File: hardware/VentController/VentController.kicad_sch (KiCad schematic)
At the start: 12 parts

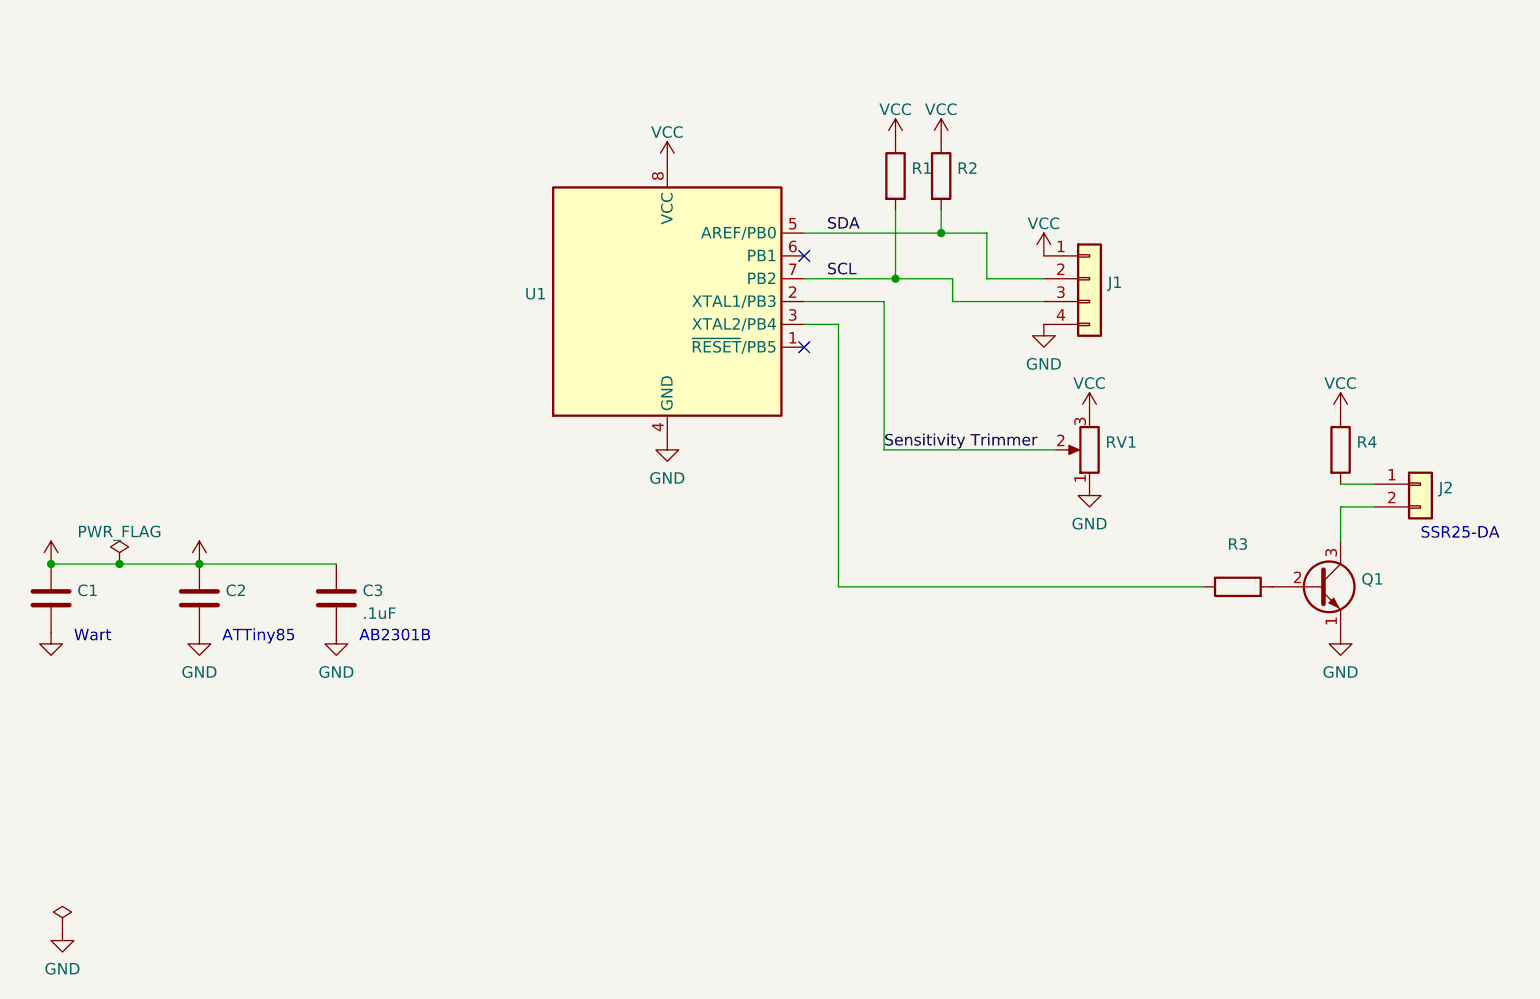
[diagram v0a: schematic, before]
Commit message: Add optional configurations to ssr
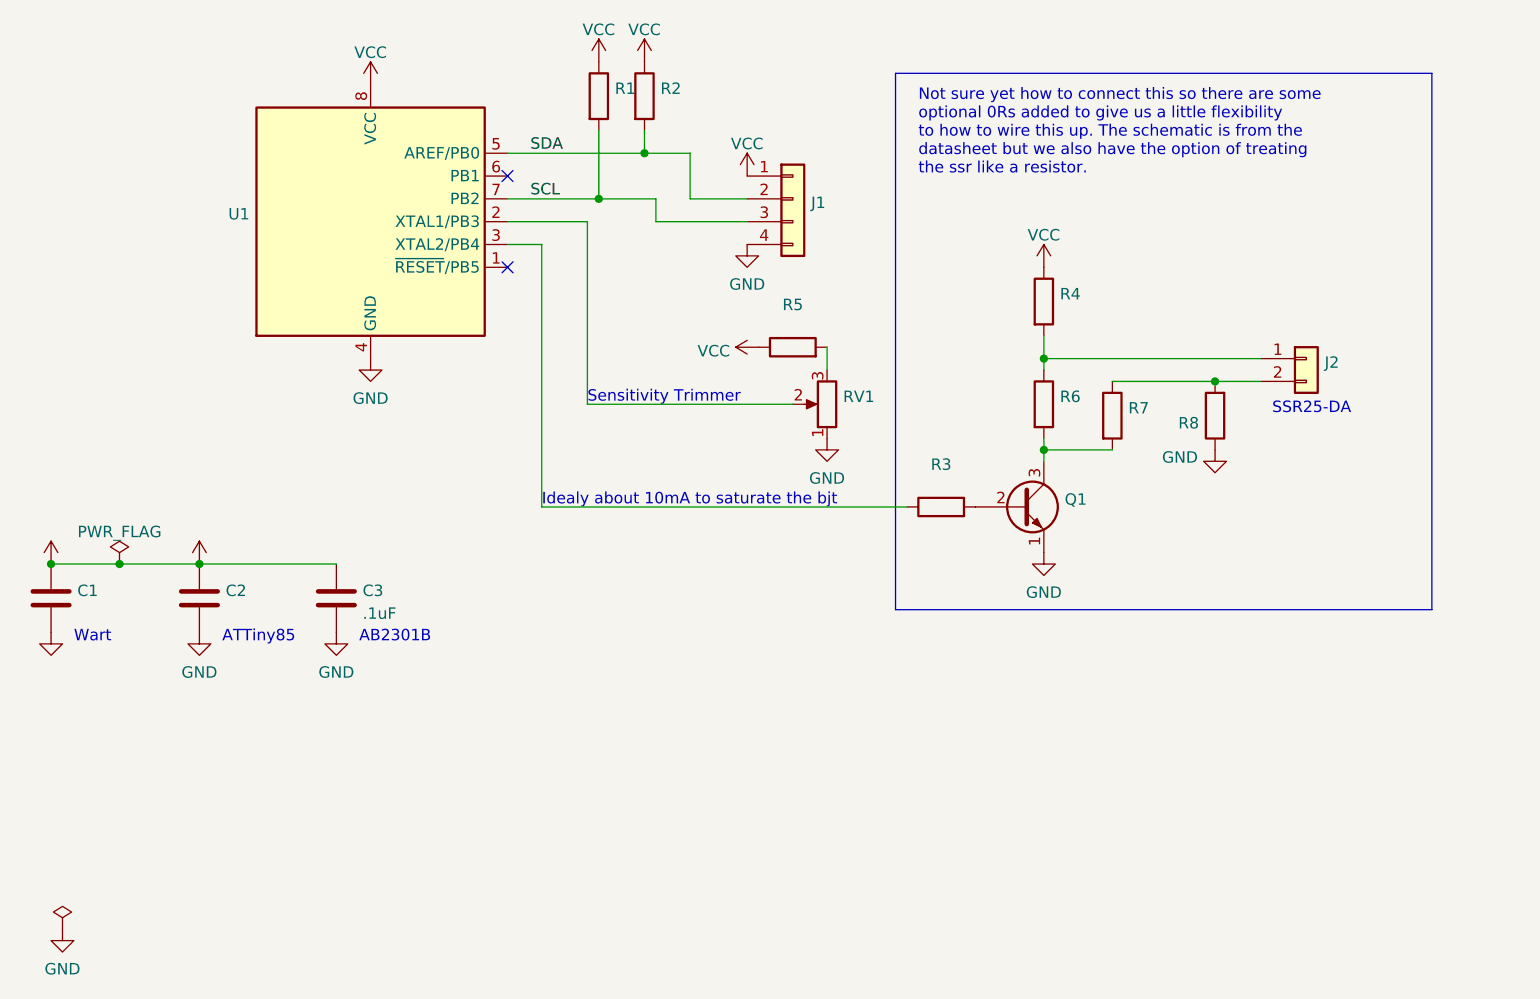
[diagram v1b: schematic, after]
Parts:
- added R5, R7, R8: (no value), Resistor_SMD:R_0805_2012Metric_Pad1.20x1.40mm_HandSolder, symbol Device:R
- added R6: (no value), symbol Device:R
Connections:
- net +5V: now also R5.1; no longer RV1.3
- net GND: now also R8.1
- net at J2.1 (Pin_1), R4.2: now also R6.1
- net at J2.2 (Pin_2): now also R7.1, R8.2; no longer Q1.3 (C)
- net Sensitivity Trimmer: no longer names the net of RV1.2, U1.2 (XTAL1/PB3)
- new net: R5.2, RV1.3
- new net: Q1.3 (C), R6.2, R7.2
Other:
- note added: "Idealy about 10mA to saturate the bjt"
- note added: "Not sure yet how to connect this so there are some optional 0Rs added to give us a little flexibility to how to wire this up. The schematic is from the datasheet but we also have the option of treating the ssr like a resistor."
- note added: "Sensitivity Trimmer"
- moved on the sheet: J1, J2, Q1, R1, R2, R3, R4, RV1, U1

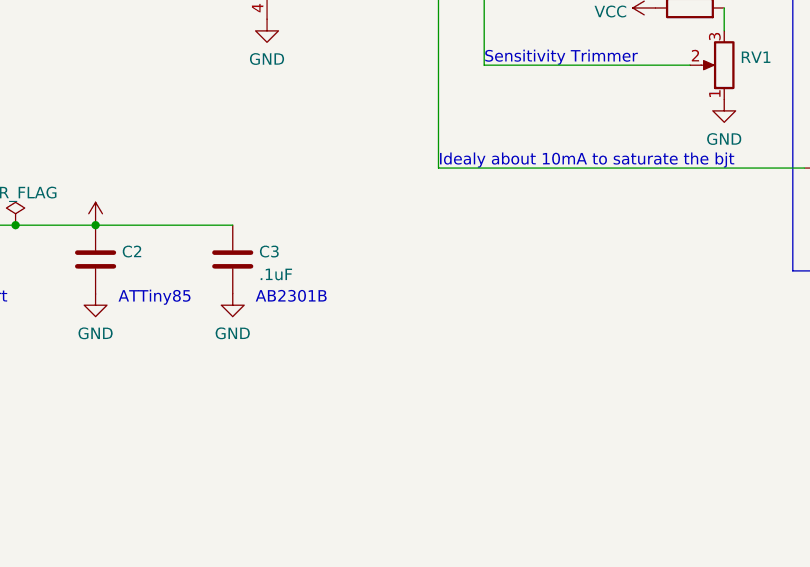
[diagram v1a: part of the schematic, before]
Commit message: Add decoupling caps for ssr and trimmer
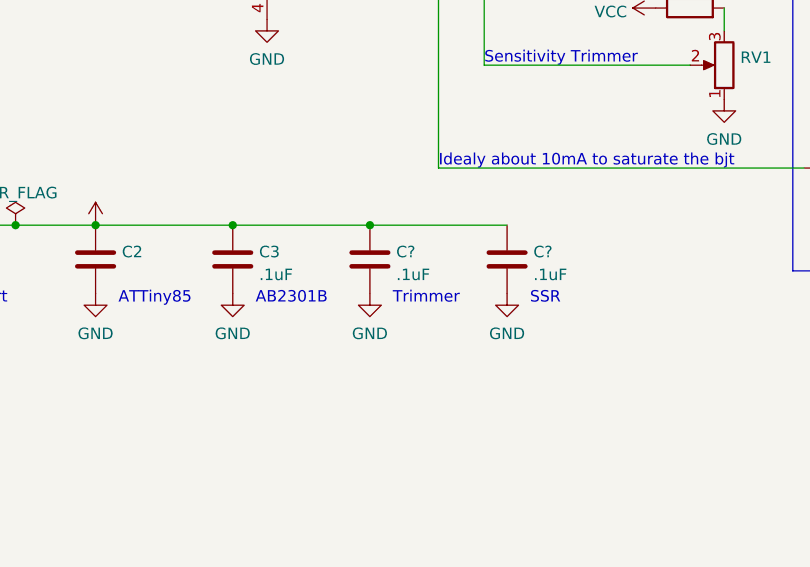
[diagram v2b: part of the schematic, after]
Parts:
- added C? (x2): .1uF, Capacitor_SMD:C_0805_2012Metric_Pad1.18x1.45mm_HandSolder, symbol Device:C
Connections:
- net +5V: now also C?.1, C?.1
- net GND: now also C?.2, C?.2
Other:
- note added: "SSR"
- note added: "Trimmer"
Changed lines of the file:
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@@
   (junction (at 92.71 34.29) (diameter 0) (color 0 0 0 0)
   )
+  (junction (at 58.42 80.01) (diameter 0) (color 0 0 0 0)
+  )
   (junction (at 137.16 57.15) (diameter 0) (color 0 0 0 0)
   )
   (junction (at 34.29 80.01) (diameter 0) (color 0 0 0 0)
+  )
+  (junction (at 73.66 80.01) (diameter 0) (color 0 0 0 0)
   )
   (junction (at 156.21 59.69) (diameter 0) (color 0 0 0 0)
@@
     (stroke (width 0) (type default) (color 0 0 0 0))
   )
+  (wire (pts (xy 73.66 80.01) (xy 88.9 80.01))
+    (stroke (width 0) (type default) (color 0 0 0 0))
+  )
   (wire (pts (xy 86.36 62.23) (xy 109.22 62.23))
     (stroke (width 0) (type default) (color 0 0 0 0))
@@
   )
   (wire (pts (xy 77.47 39.37) (xy 87.63 39.37))
+    (stroke (width 0) (type default) (color 0 0 0 0))
+  )
+  (wire (pts (xy 58.42 80.01) (xy 73.66 80.01))
     (stroke (width 0) (type default) (color 0 0 0 0))
   )
@@
     )
   )
+  (text "Trimmer\n" (at 76.2 88.9 0)
+    (effects (font (size 1.27 1.27)) (justify left bottom))
+  )
   (text "Sensitivity Trimmer" (at 86.36 62.23 0)
     (effects (font (size 1.27 1.27)) (justify left bottom))
@@
   )
   (text "Wart" (at 29.21 88.9 0)
+    (effects (font (size 1.27 1.27)) (justify left bottom))
+  )
+  (text "SSR\n" (at 91.44 88.9 0)
     (effects (font (size 1.27 1.27)) (justify left bottom))
   )
@@
     (pin "1")
   )
+  (symbol (lib_id "power:GND") (at 88.9 87.63 0) (unit 1)
+    (in_bom yes) (on_board yes) (fields_autoplaced)
+    (property "Reference" "#PWR?" (id 0) (at 88.9 93.98 0)
+      (effects (font (size 1.27 1.27)) hide)
+    )
+    (property "Value" "GND" (id 1) (at 88.9 92.0734 0))
+    (property "Footprint" "" (id 2) (at 88.9 87.63 0)
+      (effects (font (size 1.27 1.27)) hide)
+    )
+    (property "Datasheet" "" (id 3) (at 88.9 87.63 0)
+      (effects (font (size 1.27 1.27)) hide)
+    )
+    (pin "1")
+  )
   (symbol (lib_id "power:GND") (at 113.03 66.04 0) (unit 1)
     (in_bom yes) (on_board yes) (fields_autoplaced)
@@
     (pin "2")
   )
+  (symbol (lib_id "Device:C") (at 73.66 83.82 0) (unit 1)
+    (in_bom yes) (on_board yes) (fields_autoplaced)
+    (property "Reference" "C?" (id 0) (at 76.581 82.9853 0)
+      (effects (font (size 1.27 1.27)) (justify left))
+    )
+    (property "Value" ".1uF" (id 1) (at 76.581 85.5222 0)
+      (effects (font (size 1.27 1.27)) (justify left))
+    )
+    (property "Footprint" "Capacitor_SMD:C_0805_2012Metric_Pad1.18x1.45mm_HandSolder" (id 2) (at 74.6252 87.63 0)
+      (effects (font (size 1.27 1.27)) hide)
+    )
+    (property "Datasheet" "~" (id 3) (at 73.66 83.82 0)
+      (effects (font (size 1.27 1.27)) hide)
+    )
+    (pin "1")
+    (pin "2")
+  )
   (symbol (lib_id "power:GND") (at 58.42 87.63 0) (unit 1)
     (in_bom yes) (on_board yes) (fields_autoplaced)
@@
     (pin "2")
   )
+  (symbol (lib_id "power:GND") (at 73.66 87.63 0) (unit 1)
+    (in_bom yes) (on_board yes) (fields_autoplaced)
+    (property "Reference" "#PWR?" (id 0) (at 73.66 93.98 0)
+      (effects (font (size 1.27 1.27)) hide)
+    )
+    (property "Value" "GND" (id 1) (at 73.66 92.0734 0))
+    (property "Footprint" "" (id 2) (at 73.66 87.63 0)
+      (effects (font (size 1.27 1.27)) hide)
+    )
+    (property "Datasheet" "" (id 3) (at 73.66 87.63 0)
+      (effects (font (size 1.27 1.27)) hide)
+    )
+    (pin "1")
+  )
+  (symbol (lib_id "Device:C") (at 88.9 83.82 0) (unit 1)
+    (in_bom yes) (on_board yes) (fields_autoplaced)
+    (property "Reference" "C?" (id 0) (at 91.821 82.9853 0)
+      (effects (font (size 1.27 1.27)) (justify left))
+    )
+    (property "Value" ".1uF" (id 1) (at 91.821 85.5222 0)
+      (effects (font (size 1.27 1.27)) (justify left))
+    )
+    (property "Footprint" "Capacitor_SMD:C_0805_2012Metric_Pad1.18x1.45mm_HandSolder" (id 2) (at 89.8652 87.63 0)
+      (effects (font (size 1.27 1.27)) hide)
+    )
+    (property "Datasheet" "~" (id 3) (at 88.9 83.82 0)
+      (effects (font (size 1.27 1.27)) hide)
+    )
+    (pin "1")
+    (pin "2")
+  )
   (sheet_instances
     (path "/" (page "1"))
@@
       (reference "#PWR017") (unit 1) (value "GND") (footprint "")
     )
+    (path "/65b883a7-f8ee-466f-b815-3a02492bdf71"
+      (reference "#PWR?") (unit 1) (value "GND") (footprint "")
+    )
+    (path "/fc6cb265-d9be-4c2b-ab77-dd6c5935e9d5"
+      (reference "#PWR?") (unit 1) (value "GND") (footprint "")
+    )
     (path "/f81e2caa-f7a2-40dd-8668-c447b8223c0a"
       (reference "C1") (unit 1) (value "1uF") (footprint "Capacitor_SMD:C_0805_2012Metric_Pad1.18x1.45mm_HandSolder")
@@
       (reference "C3") (unit 1) (value ".1uF") (footprint "Capacitor_SMD:C_0805_2012Metric_Pad1.18x1.45mm_HandSolder")
     )
+    (path "/bb3c9ed5-e3f9-4498-b24a-1898528d46d5"
+      (reference "C?") (unit 1) (value ".1uF") (footprint "Capacitor_SMD:C_0805_2012Metric_Pad1.18x1.45mm_HandSolder")
+    )
+    (path "/fcd0c6b2-8872-4fcb-ae27-f6c287e9791c"
+      (reference "C?") (unit 1) (value ".1uF") (footprint "Capacitor_SMD:C_0805_2012Metric_Pad1.18x1.45mm_HandSolder")
+    )
     (path "/a0c0156d-8f3c-4c82-999f-49c9d8d8e545"

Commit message: Add power jack
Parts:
- added J3: (no value), symbol Connector:Barrel_Jack
- gave numbers to parts that had none: 2
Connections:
- net +5V: now also J3.1
- net GND: now also J3.2
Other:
- moved on the sheet: R2

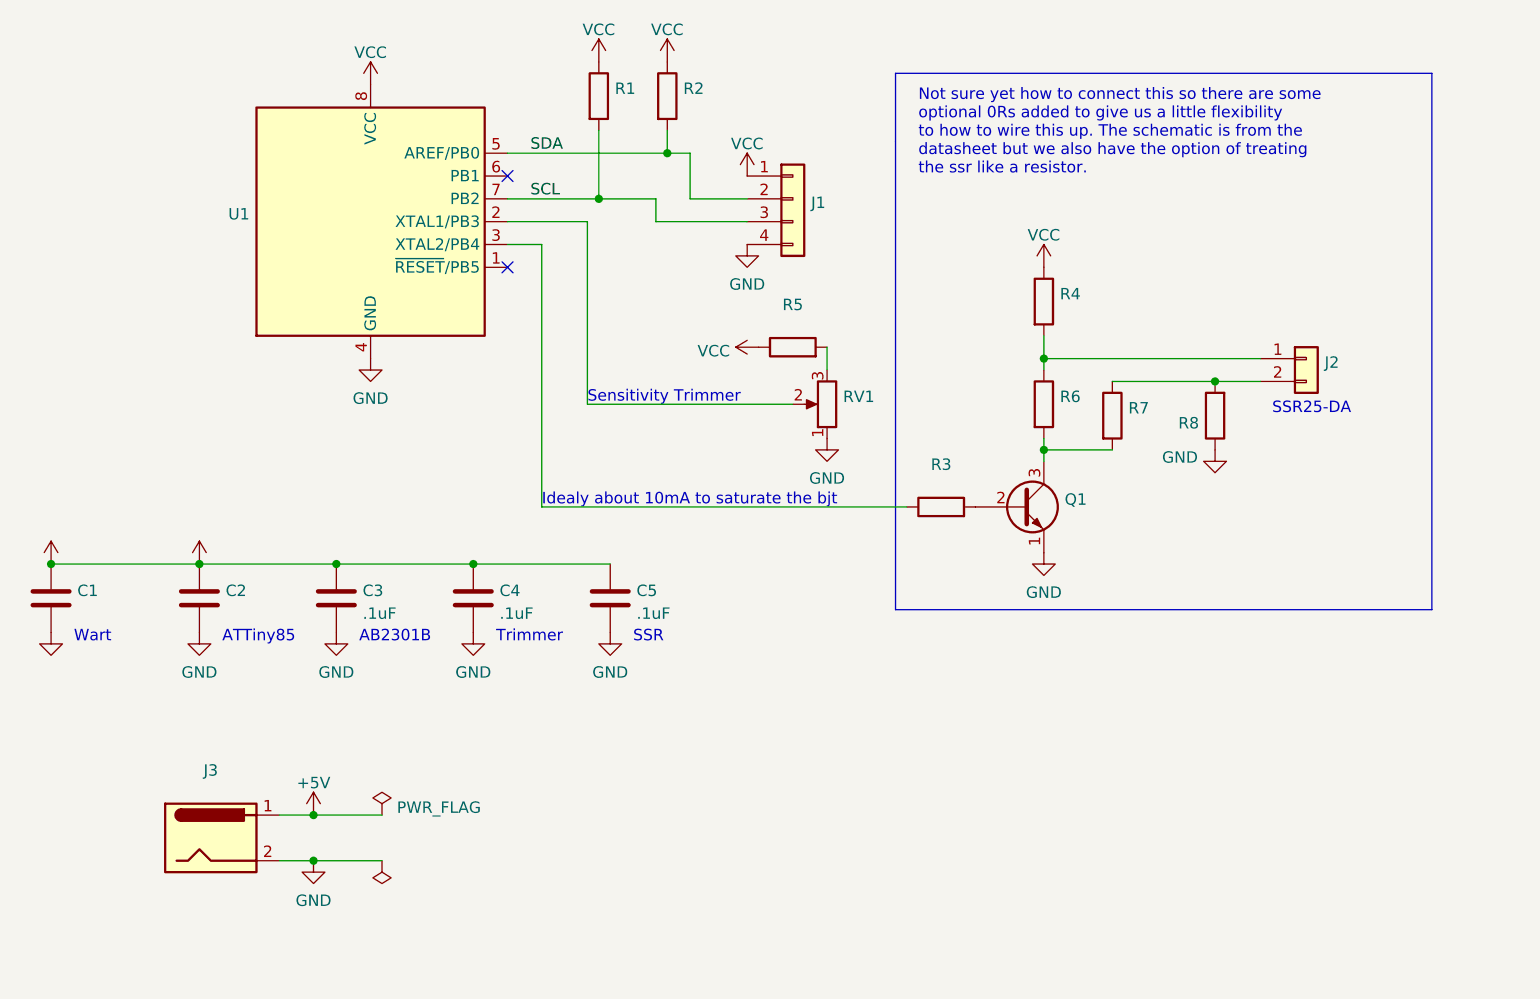
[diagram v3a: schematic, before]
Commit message: Set pcb board edges
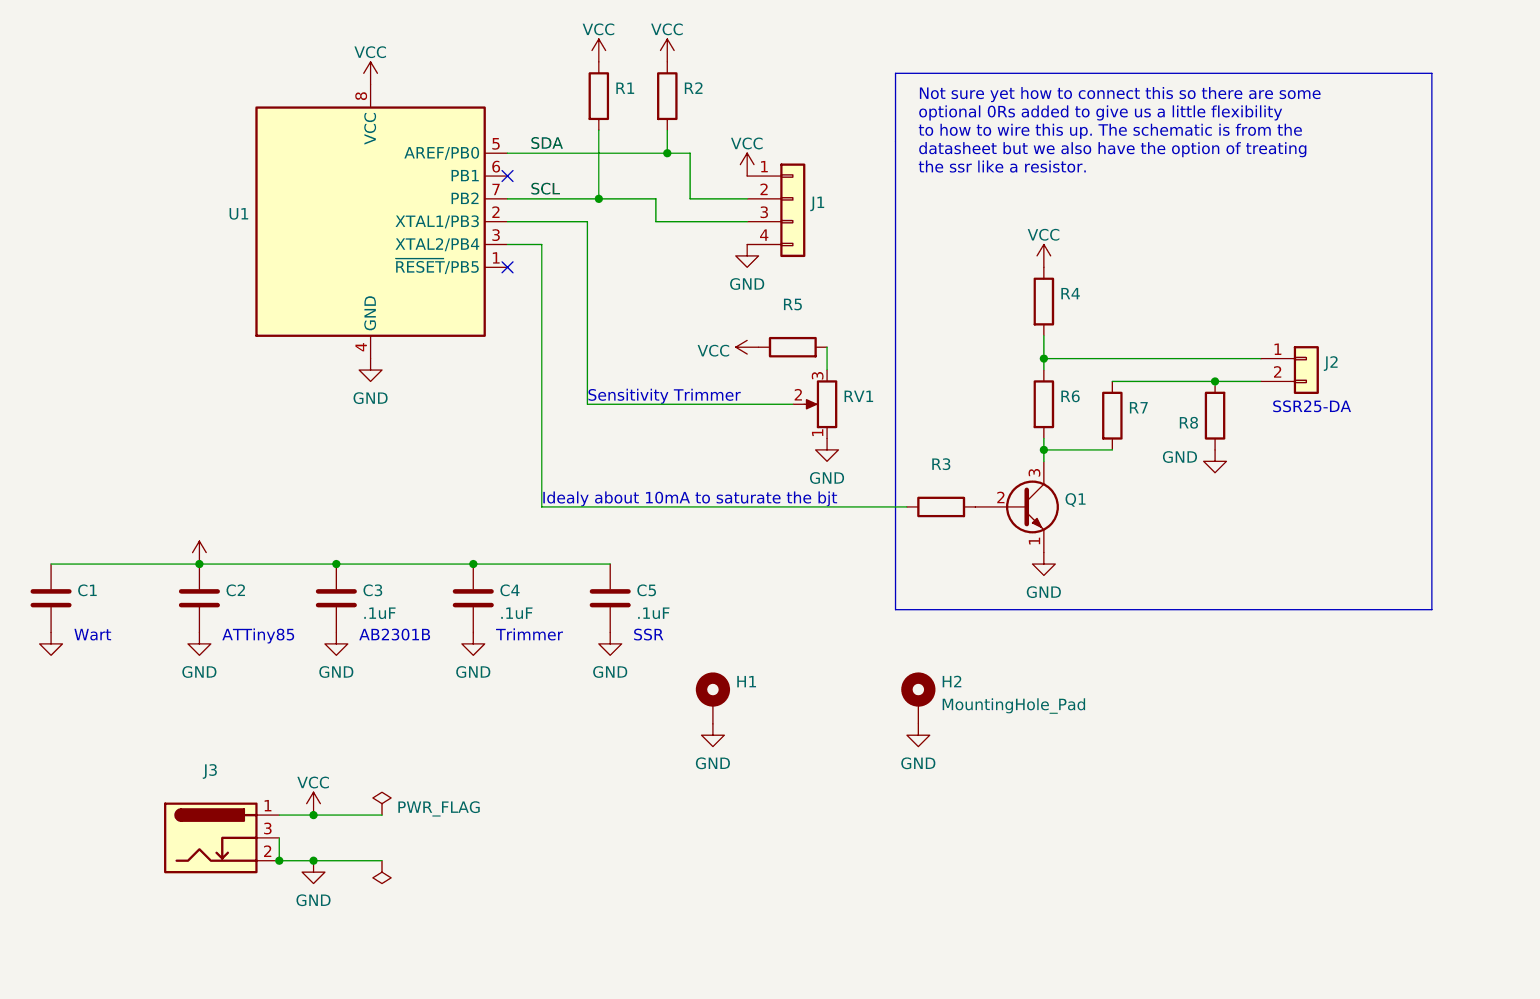
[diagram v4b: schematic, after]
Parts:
- removed J3: (no value), symbol Connector:Barrel_Jack
- added H1: (no value), symbol Mechanical:MountingHole_Pad
- added H2: MountingHole_Pad, symbol Mechanical:MountingHole_Pad
- added J3: (no value), symbol Connector:Barrel_Jack_Switch
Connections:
- net GND: now also H1.1, H2.1, J3.2, J3.3
- net +5V renamed VCC
- net VCC: now also J3.1

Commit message: Lay out pcb
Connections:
- net SCL: now also J1.2 (Pin_2); no longer J1.3 (Pin_3)
- net SDA: now also J1.3 (Pin_3); no longer J1.2 (Pin_2)
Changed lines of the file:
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@@
-    (stroke (width 0) (type default) (color 0 0 0 0))
-  )
-  (wire (pts (xy 93.98 41.91) (xy 104.14 41.91))
     (stroke (width 0) (type default) (color 0 0 0 0))
   )
@@
     (stroke (width 0) (type default) (color 0 0 0 0))
   )
-  (wire (pts (xy 87.63 39.37) (xy 93.98 39.37))
+  (wire (pts (xy 87.63 39.37) (xy 104.14 39.37))
     (stroke (width 0) (type default) (color 0 0 0 0))
   )
@@
     (stroke (width 0) (type default) (color 0 0 0 0))
   )
-  (wire (pts (xy 97.79 34.29) (xy 97.79 39.37))
+  (wire (pts (xy 97.79 34.29) (xy 97.79 41.91))
     (stroke (width 0) (type default) (color 0 0 0 0))
   )
@@
   )
   (wire (pts (xy 52.07 110.49) (xy 52.07 113.03))
+    (stroke (width 0) (type default) (color 0 0 0 0))
+  )
+  (wire (pts (xy 97.79 41.91) (xy 104.14 41.91))
     (stroke (width 0) (type default) (color 0 0 0 0))
   )
@@
     (stroke (width 0) (type default) (color 0 0 0 0))
   )
-  (wire (pts (xy 93.98 39.37) (xy 93.98 41.91))
-    (stroke (width 0) (type default) (color 0 0 0 0))
-  )
   (wire (pts (xy 95.25 31.75) (xy 95.25 34.29))
     (stroke (width 0) (type default) (color 0 0 0 0))
@@
     (stroke (width 0) (type default) (color 0 0 0 0))
   )
-  (wire (pts (xy 97.79 39.37) (xy 104.14 39.37))
-    (stroke (width 0) (type default) (color 0 0 0 0))
-  )
